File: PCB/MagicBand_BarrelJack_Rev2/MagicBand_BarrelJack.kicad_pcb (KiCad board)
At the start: 2 copper layers, 40 x 40 mm, 22 parts, among them J2 PinSocket_1x08_P2.54mm_Vertic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, J3 PinHeader_1x04_P2.54mm_Vertic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, J6 JST_PH_B3B-PH-K_1x03_P2.00mm_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, J8 PinHeader_1x02_P2.54mm_Vertic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, J9 IDC-Header_2x03_P2.54mm_Verti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, Q1 SOT-23, U1 DIP-28_W7.62mm, U2 SOT-23, Y1 Crystal_HC49-4H_Vertical

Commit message: Resize Rev2 outline to 37x25mm; confirm JST footprint, poka-yoke plan; flag DIP-28 blocker
Rev2 board outline resized from 40x40mm to the new 37x25mm target
(verified closed rectangle, correct dimensions). No component
repositioning yet -- paused before going further.

Confirmed the 1.25mm JST GH-class connector @user found on Amazon
matches real, verified KiCad library footprints (Connector_JST.pretty,
multiple pin counts/orientations) -- no placeholder needed. Logged the
male/female poka-yoke plan for the two LED-strip ports.

Found and logged a real blocker: U1's bare DIP-28 package measures
35.7mm long (from its own footprint geometry), leaving no realistic
margin on a 37mm-wide board. Flagged as needing a decision (SMD MCU
vs. revisit board size) before any further placement work.

Co-Authored-By: Claude Sonnet 5 <noreply@anthropic.com>
Claude-Session: https://claude.ai/code/session_01UiULxbNnG293uuE4csn9nG
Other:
- board size 40 x 40 mm -> 37 x 25 mm
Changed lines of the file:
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@@
 	(gr_line
 		(start 0 0)
-		(end 40 0)
+		(end 37 0)
 		(stroke
 			(width 0.15)
@@
 	)
 	(gr_line
-		(start 0 40)
+		(start 0 25)
 		(end 0 0)
 		(stroke
@@
 	)
 	(gr_line
-		(start 40 0)
-		(end 40 40)
+		(start 37 0)
+		(end 37 25)
 		(stroke
 			(width 0.15)
@@
 	)
 	(gr_line
-		(start 40 40)
-		(end 0 40)
+		(start 37 25)
+		(end 0 25)
 		(stroke
 			(width 0.15)

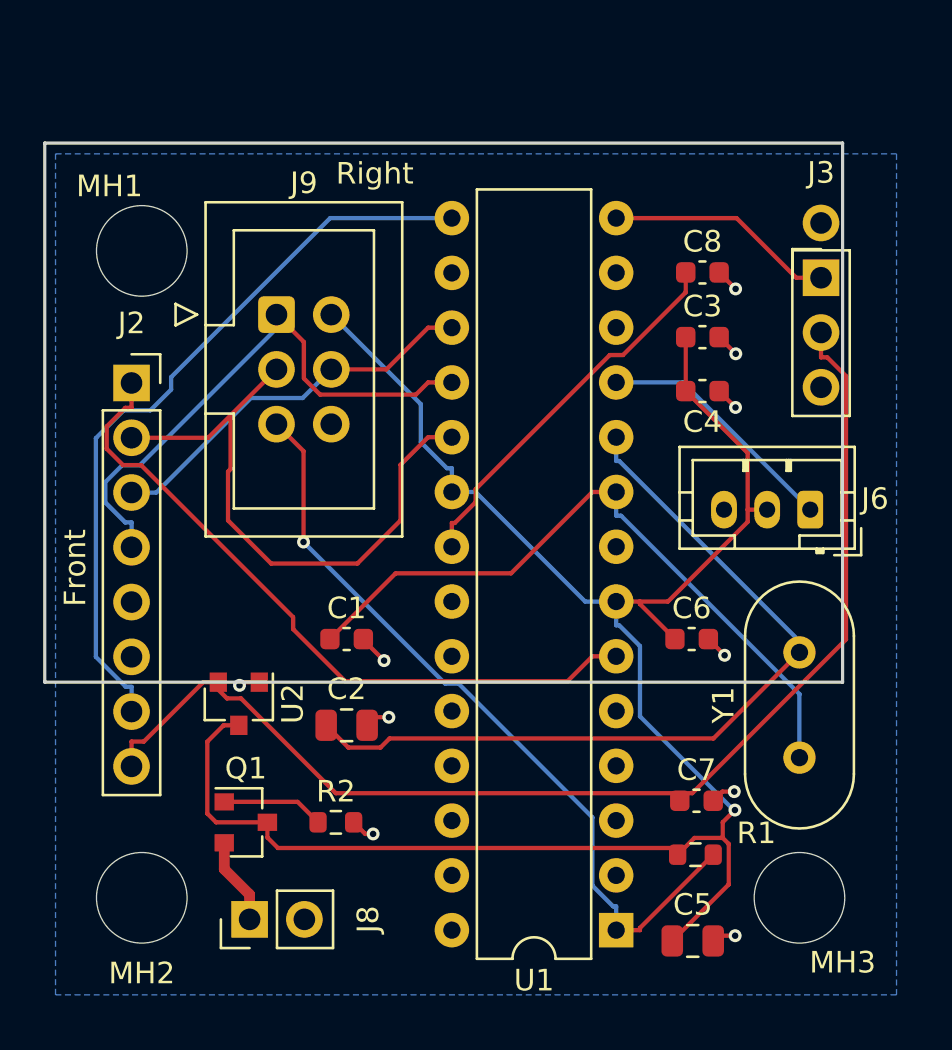
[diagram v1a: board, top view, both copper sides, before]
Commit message: Rev 2 draft: U1 swapped to TQFP-32, routing stripped, rough placement
PCB-side work only (schematic untouched), done per @user's explicit
request to populate a draft for later GUI verification:

- U1 footprint swapped DIP-28 -> TQFP-32, 20/32 pads individually
  net-assigned matching the real current net names. D2 and D3
  (SWITCH) wired as real nets for the first time -- previously only
  physical bodge wires, never in the design files.
- Stripped 177 stale track segments, 12 vias, 3 GND-zone fill
  polygons -- rev 1 was fully routed, moving U1 left everything
  dangling at old pad positions. GND zone outline resized to the new
  37x25mm board.
- Repositioned all 21 existing footprints into the new outline.
  NOT DRC-clean: 15 courtyard overlaps and assorted clearance/shorting
  violations remain, honestly reported, not glossed over. Needs a
  real GUI placement pass.
- New connector footprints (LED strip x2, momentary switch) not yet
  added -- only their nets are reserved on U1.

Co-Authored-By: Claude Sonnet 5 <noreply@anthropic.com>
Claude-Session: https://claude.ai/code/session_01UiULxbNnG293uuE4csn9nG
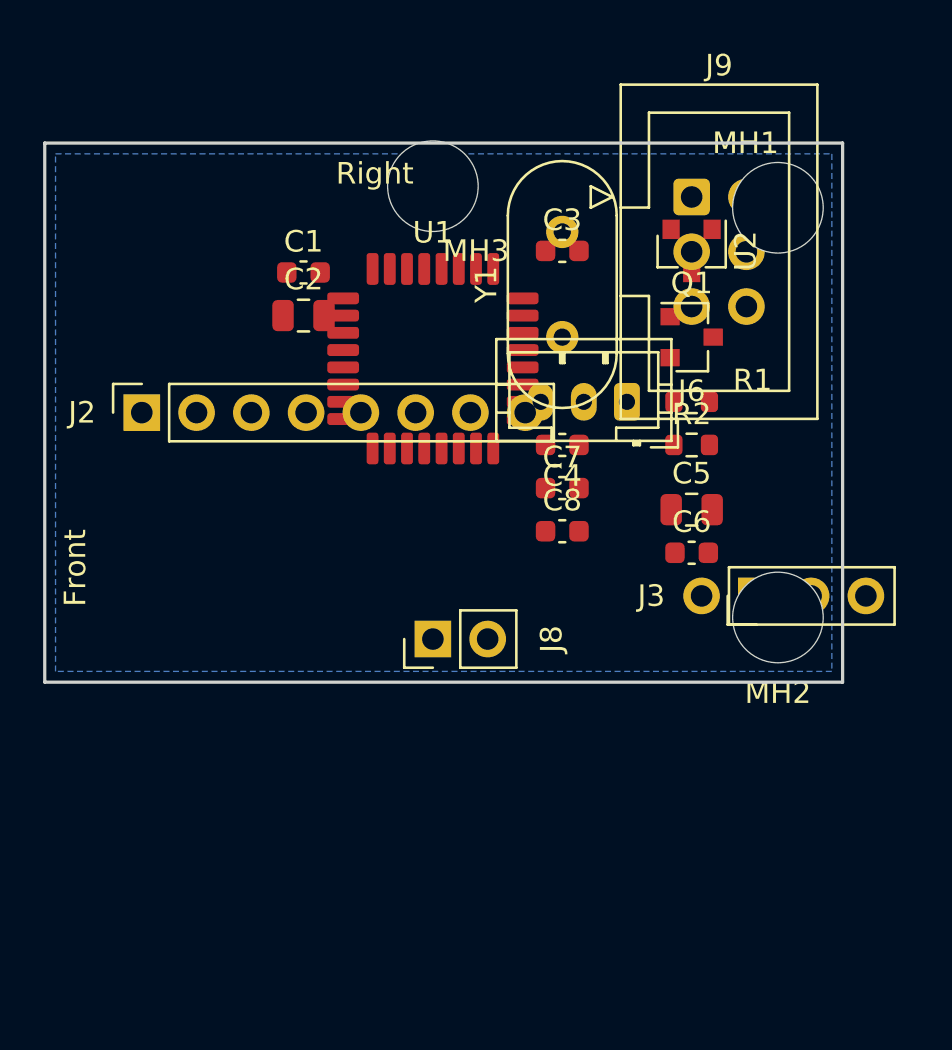
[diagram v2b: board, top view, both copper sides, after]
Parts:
- U1: value DIP-28_W7.62mm -> ATmega328P-A; footprint DIP-28_W7.62mm -> TQFP-32_7x7mm_P0.8mm
- moved MH3 37.1 mm to (18.0, 2.00)
- moved MH2 32.2 mm to (34.0, 22.0)
- moved Q1 30.6 mm to (30.0, 9.00)
- moved U2 29.7 mm to (30.0, 5.00)
- moved MH1 29.6 mm to (34.0, 3.00)
- moved U1 27.8 mm to (18.0, 10.0), turned to 0 degrees
- moved R2 24.1 mm to (30.0, 14.0)
- moved Y1 22.4 mm to (24.0, 9.00)
- moved R1 21.0 mm to (30.0, 12.0)
- moved J9 20.0 mm to (30.0, 2.50)
- moved C5 20.0 mm to (30.0, 17.0)
- moved C2 19.1 mm to (12.0, 8.00)
- moved C1 17.1 mm to (12.0, 6.00)
- moved C7 15.8 mm to (24.0, 16.0)
- moved J8 15.5 mm to (18.0, 23.0)
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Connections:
- U1 pad 1: MCU_RESET -> SWITCH
- U1 pad 10: Net-(U1-XTAL2/PB7) -> D6
- U1 pad 11: D5 -> unconnected-(U1-pin11)
- U1 pad 12: D6 -> D8
- U1 pad 13: unconnected-(U1-PD7-Pad13) -> D9
- U1 pad 14: D8 -> unconnected-(U1-pin14)
- U1 pad 15: D9 -> D11
- U1 pad 16: unconnected-(U1-PB2-Pad16) -> D12
- U1 pad 17: D11 -> D13
- U1 pad 18: D12 -> +5V
- U1 pad 19: D13 -> unconnected-(U1-pin19)
- U1 pad 2: unconnected-(U1-PD0-Pad2) -> D4
- U1 pad 20: +5V -> Net-(U1-AREF)
- U1 pad 21: Net-(U1-AREF) -> GND
- U1 pad 22: GND -> unconnected-(U1-pin22)
- U1 pad 3: unconnected-(U1-PD1-Pad3) -> GND
- U1 pad 4: unconnected-(U1-PD2-Pad4) -> +5V
- U1 pad 5: unconnected-(U1-PD3-Pad5) -> GND
- U1 pad 6: D4 -> +5V
- U1 pad 7: +5V -> Net-(U1-XTAL1/PB6)
- U1 pad 8: GND -> Net-(U1-XTAL2/PB7)
- U1 pad 9: Net-(U1-XTAL1/PB6) -> D5
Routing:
- net +5V: track 91.2 -> 0.00 mm, vias 1 -> 0
- net +3V3: track 56.1 -> 0.00 mm
- net Net-(U1-XTAL2/PB7): track 37.8 -> 0.00 mm
- net MCU_RESET: track 36.4 -> 0.00 mm, vias 1 -> 0
- net D9: track 34.6 -> 0.00 mm
- net D4: track 32.6 -> 0.00 mm
- net Net-(U1-XTAL1/PB6): track 32.1 -> 0.00 mm
- net D13: track 28.1 -> 0.00 mm
- net D12: track 26.1 -> 0.00 mm
- net D11: track 18.0 -> 0.00 mm
- net Net-(U1-AREF): track 17.7 -> 0.00 mm
- net GND: track 11.5 -> 0.00 mm, vias 10 -> 0
- net D5: track 11.4 -> 0.00 mm
- net D8: track 10.6 -> 0.00 mm
- net Net-(Q1-Pin_1): track 4.74 -> 0.00 mm
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
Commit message: Rev 2: add all 3 new connectors + spare-pin breakout, fix poka-yoke plan
J6 (outer LED) swapped from 2.0mm JST-PH to real 3-pin JST GH. Added
J10 (inner LED, 4-pin GH, pin 4 unused), J11 (momentary switch, 2-pin
GH), J12 (spare-pin breakout, 4-pin GH: D7/D10/RXD/TXD). D2, SWITCH,
D7, D10, RXD, TXD are now real nets in the design files for the first
time.

Corrected the poka-yoke plan: confirmed JST GH has no female PCB-mount
receptacle (checked on disk, not assumed) -- switched from mismatched
connector gender to mismatched pin count, same impossible-to-swap
goal, parts that actually exist.

Recommended keeping J9 (ISP) at its current 2.54mm size rather than
shrinking it -- real tooling/cable investment already sunk, and the
actual space problems (old DIP-28, old 2.0mm LED connector) are
already fixed elsewhere.

Caught and fixed a real insertion bug (naive string search split J6's
block in half) via the file failing to parse -- reverted and redid
with proper balanced-paren extraction.

DRC after: courtyard overlaps dropped 15->8 overall, but the 3 new
connectors are tightly packed against each other/neighbors. Stopped
manual fixes once they started revealing new collisions instead of
resolving them -- confirmed GUI-iteration territory.

Co-Authored-By: Claude Sonnet 5 <noreply@anthropic.com>
Claude-Session: https://claude.ai/code/session_01UiULxbNnG293uuE4csn9nG
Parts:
- added J10: LED_INNER_RING_4P, JST_GH_BM04B-GHS-TBT_1x04-1MP_P1.25mm_Vertical, F.Cu at (28.0, 17.0)
- added J11: SWITCH_2P, JST_GH_BM02B-GHS-TBT_1x02-1MP_P1.25mm_Vertical, F.Cu at (11.0, 19.0)
- added J12: SPARE_BREAKOUT_4P, JST_GH_BM04B-GHS-TBT_1x04-1MP_P1.25mm_Vertical, F.Cu at (8.00, 20.0)
- J6: value JST_PH_B3B-PH-K_1x03_P2.00mm_Vertical -> LED_OUTER_RING_3P; footprint JST_PH_B3B-PH-K_1x03_P2.00mm_Vertical -> JST_GH_BM03B-GHS-TBT_1x03-1MP_P1.25mm_Vertical
- moved J6 2.24 mm to (28.0, 10.0), turned to 0 degrees
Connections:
- J6 pad 1: D5 -> +5V
- J6 pad 2: +5V -> GND
- J6 pad 3: GND -> D5
- U1 pad 11: unconnected-(U1-pin11) -> D7
- U1 pad 14: unconnected-(U1-pin14) -> D10
- U1 pad 30: unconnected-(U1-pin30) -> RXD
- U1 pad 31: unconnected-(U1-pin31) -> TXD
